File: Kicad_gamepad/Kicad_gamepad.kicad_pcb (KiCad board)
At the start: 2 copper layers, 40 parts, among them J1 USB_A, J2 Conn_01x05_Pin, SW1 SW_Push, U1 PIC18F4550-IPT, Y1 Crystal, Y2 SW_Push, x1 SW_Push

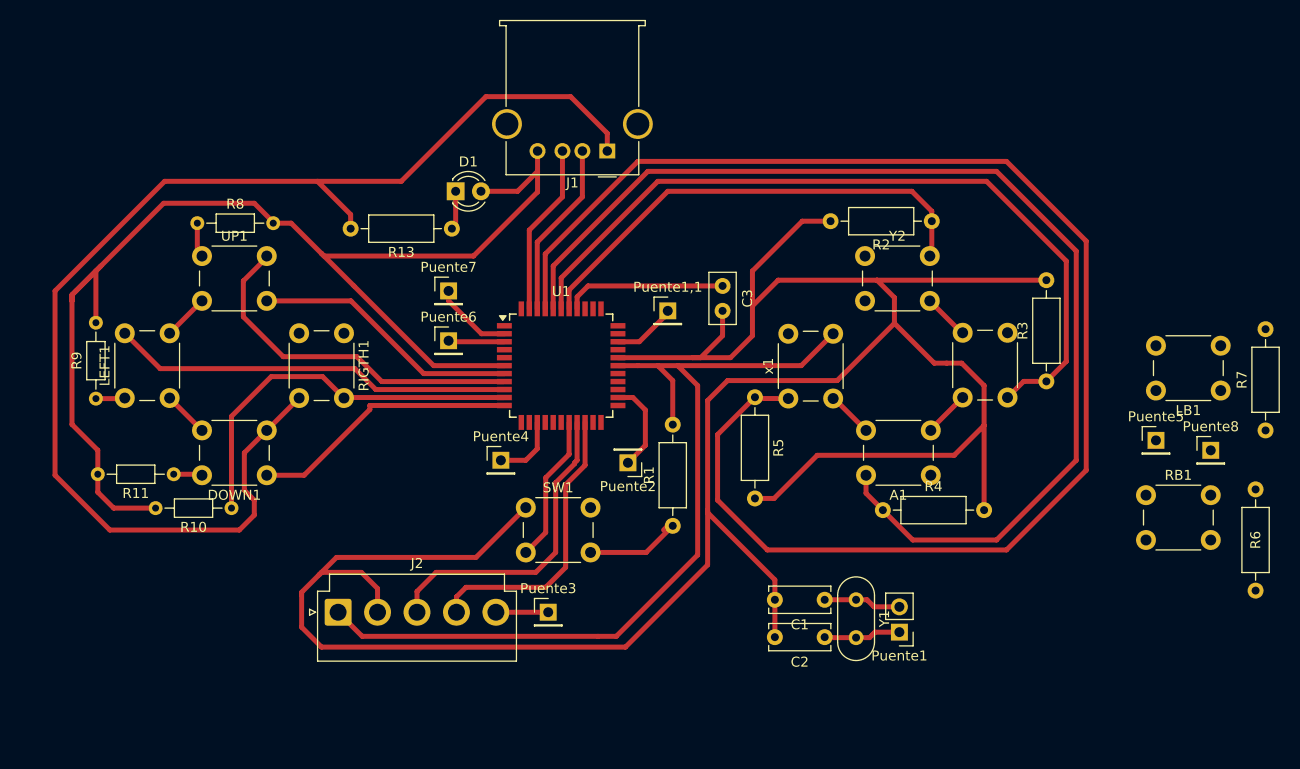
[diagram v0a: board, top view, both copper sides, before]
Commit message: Kicad verción Actual
Pickit Considerado
pistas con respecto a ditancias reales
PCB prototipa fabricada
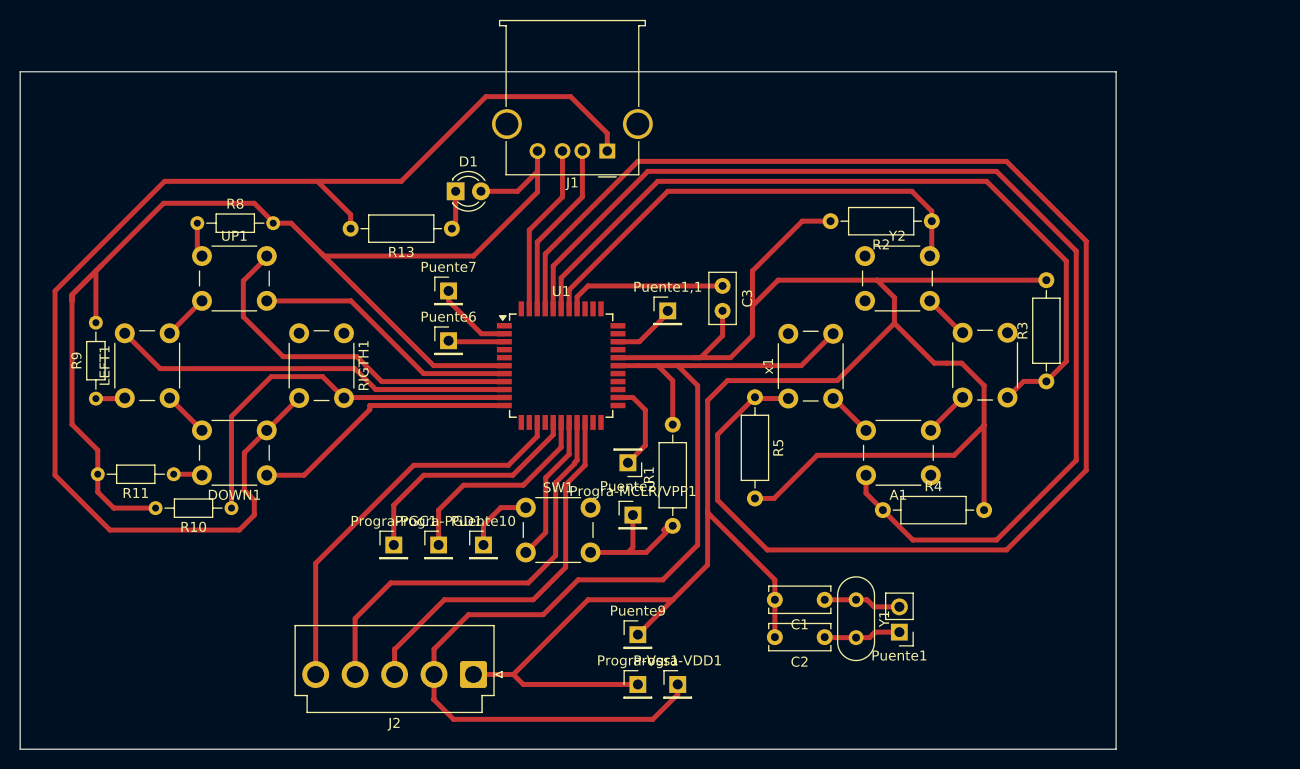
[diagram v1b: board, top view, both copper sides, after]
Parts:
- removed LB1, RB1: SW_Push, Button_Switch_THT:SW_PUSH_6mm
- removed Puente3, Puente4: Puente3, Connector_PinHeader_2.54mm:PinHeader_1x01_P2.54mm_Vertical
- removed Puente5: Puente5, Connector_PinHeader_2.54mm:PinHeader_1x01_P2.54mm_Vertical
- removed Puente8: Puente7, Connector_PinHeader_2.54mm:PinHeader_1x01_P2.54mm_Vertical
- removed R6, R7: R, Resistor_THT:R_Axial_DIN0207_L6.3mm_D2.5mm_P10.16mm_Horizontal
- added Progra-MCLR/VPP1: Programador, Connector_PinHeader_2.54mm:PinHeader_1x01_P2.54mm_Vertical, F.Cu at (136.8, 115.2)
- added Progra-PGC1: Programador, Connector_PinHeader_2.54mm:PinHeader_1x01_P2.54mm_Vertical, F.Cu at (112.8, 118.2)
- added Progra-PGD1: Programador, Connector_PinHeader_2.54mm:PinHeader_1x01_P2.54mm_Vertical, F.Cu at (117.2, 118.2)
- added Progra-VDD1: Programador, Connector_PinHeader_2.54mm:PinHeader_1x01_P2.54mm_Vertical, F.Cu at (141.2, 132.2)
- added Progra-Vss1: Programador, Connector_PinHeader_2.54mm:PinHeader_1x01_P2.54mm_Vertical, F.Cu at (137.2, 132.2)
- added Puente10: Puente9, Connector_PinHeader_2.54mm:PinHeader_1x01_P2.54mm_Vertical, F.Cu at (121.8, 118.2)
- added Puente9: Puente9, Connector_PinHeader_2.54mm:PinHeader_1x01_P2.54mm_Vertical, F.Cu at (137.2, 127.2)
- moved J2 15.0 mm to (120.8, 131.2), turned to 180 degrees
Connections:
- A1 pad 2: Net-(J2-Pin_1) -> Net-(J2-Pin_2)
- B1 pad 2: Net-(J2-Pin_1) -> Net-(J2-Pin_2)
- C1 pad 2: Net-(J2-Pin_2) -> Net-(J2-Pin_1)
- C2 pad 2: Net-(J2-Pin_2) -> Net-(J2-Pin_1)
- C3 pad 2: Net-(J2-Pin_2) -> Net-(J2-Pin_1)
- R1 pad 2: Net-(J2-Pin_1) -> Net-(J2-Pin_2)
- R2 pad 2: Net-(J2-Pin_2) -> Net-(J2-Pin_1)
- R3 pad 2: Net-(J2-Pin_2) -> Net-(J2-Pin_1)
- R4 pad 2: Net-(J2-Pin_2) -> Net-(J2-Pin_1)
- R5 pad 2: Net-(J2-Pin_2) -> Net-(J2-Pin_1)
- SW1 pad 1: Net-(J2-Pin_2) -> Net-(Puente10-Pin_1)
- U1 pad 14: Net-(Puente4-Pin_1) -> Net-(J2-Pin_5)
- U1 pad 16: unconnected-(U1-RB6/KBI2/PGC-Pad16) -> Net-(Progra-PGC1-Pin_1)
- U1 pad 17: unconnected-(U1-RB7/KBI3/PGD-Pad17) -> Net-(Progra-PGD1-Pin_1)
- U1 pad 19: Net-(J2-Pin_3) -> Net-(J2-Pin_4)
- U1 pad 20: Net-(J2-Pin_4) -> Net-(J2-Pin_3)
- U1 pad 28: Net-(J2-Pin_1) -> Net-(J2-Pin_2)
- U1 pad 29: Net-(J2-Pin_2) -> Net-(J2-Pin_1)
- Y2 pad 2: Net-(J2-Pin_1) -> Net-(J2-Pin_2)
- x1 pad 2: Net-(J2-Pin_1) -> Net-(J2-Pin_2)
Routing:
- net Net-(J2-Pin_2): track 260.5 -> 125.4 mm
- net Net-(J2-Pin_1): track 103.6 -> 222.9 mm
- net Net-(J2-Pin_5): track 5.25 -> 40.1 mm
- net Net-(Progra-PGC1-Pin_1): track 0.00 -> 24.2 mm
- net Net-(Progra-PGD1-Pin_1): track 0.00 -> 20.9 mm
- net Net-(J2-Pin_4): track 29.1 -> 42.6 mm
- net Net-(Puente10-Pin_1): track 0.00 -> 6.97 mm
- net Net-(J2-Pin_3): track 31.6 -> 38.5 mm
- net Net-(Puente4-Pin_1): track 6.78 -> 0.00 mm
- net Net-(Progra-MCLR/VPP1-Pin_1): track 24.8 -> 28.8 mm
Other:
- board outline added: 110 x 68 mm

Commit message: Corrección de Kicad
Versión actualizada con corrección de pistas, huellas, y tamaño de conexión.
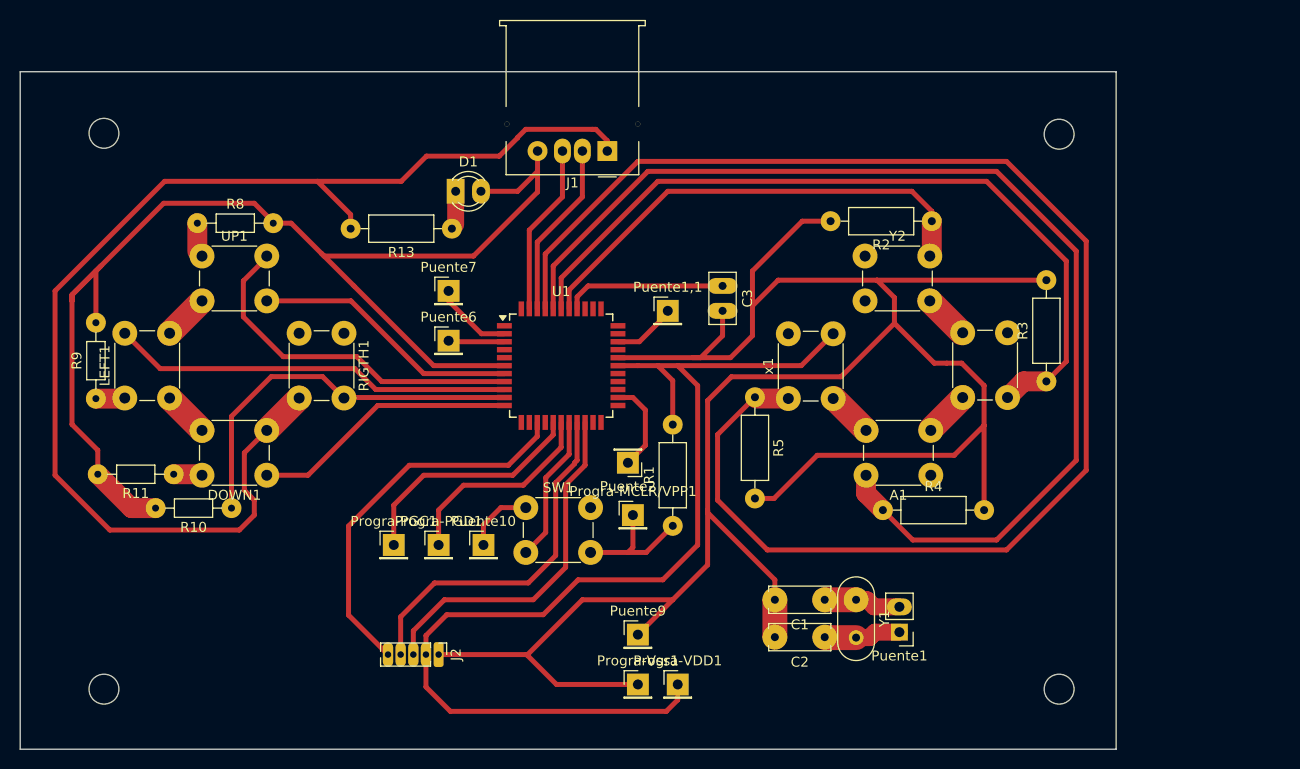
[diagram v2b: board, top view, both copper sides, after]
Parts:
- J2: footprint Connector_JST:JST_VH_B5P-VH_1x05_P3.96mm_Vertical -> Connector_PinHeader_1.27mm:PinHeader_1x05_P1.27mm_Vertical
- moved J2 4.03 mm to (117.2, 129.2), turned to -90 degrees
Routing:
- net Net-(J2-Pin_4): track 42.6 -> 36.1 mm
- net Net-(J1-VBUS): track 164.8 -> 161.7 mm
- net Net-(J2-Pin_3): track 38.5 -> 35.7 mm
- net Net-(J2-Pin_1): track 222.9 -> 225.0 mm
- net Net-(J2-Pin_5): track 40.1 -> 38.6 mm
- net Net-(J2-Pin_2): track 125.4 -> 126.7 mm
- net Net-(D1-A): track 126.3 -> 125.3 mm
- net Net-(Progra-MCLR/VPP1-Pin_1): track 28.8 -> 28.2 mm
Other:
- outline, holes or cut-outs redrawn

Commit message: kicad final
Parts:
- J2: footprint Connector_PinHeader_1.27mm:PinHeader_1x05_P1.27mm_Vertical -> Connector_PinHeader_2.54mm:PinHeader_1x05_P2.54mm_Vertical
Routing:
- net Net-(J2-Pin_2): track 126.7 -> 140.6 mm
- net Net-(J2-Pin_4): track 36.1 -> 39.6 mm
- net Net-(J2-Pin_3): track 35.7 -> 37.9 mm
- net Net-(J2-Pin_5): track 38.6 -> 37.2 mm
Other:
- board size 110 x 68 mm -> 110 x 65.9 mm

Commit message: Kicad Gatillos
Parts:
- moved Puente2 14.3 mm to (142.2, 96.9)
- moved Puente1,1 1.79 mm to (138.5, 94.8)
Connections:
- U1 pad 24: Net-(Puente2-Pin_1) -> unconnected-(U1-RA5/AN4/~{SS}/HLVDIN/C2OUT-Pad24)
- U1 pad 30: unconnected-(U1-OSC1/CLKI-Pad30) -> Net-(Puente2-Pin_1)
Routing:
- net Net-(Puente2-Pin_1): track 9.29 -> 7.62 mm
- net Net-(Puente1,1-Pin_1): track 6.43 -> 5.62 mm
